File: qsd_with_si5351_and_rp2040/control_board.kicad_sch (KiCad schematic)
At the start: 33 parts, among them U101 RP2040, U102 W25Q128JVS, U103 MS5351M, Y101 403C35D12M00000, Y102 MCSJK-7U-27.00-10-10-60-B-10

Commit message: schematic ~ done - try some layout
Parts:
- added D101: LED_RED, Diode_SMD:D_0805_2012Metric, symbol Device:LED_Small
- added J104: Conn_01x04, Connector_PinHeader_2.54mm:PinHeader_1x04_P2.54mm_Vertical, symbol Connector_Generic:Conn_01x04
- added J105: Conn_02x14_Odd_Even, Connector_PinSocket_2.54mm:PinSocket_2x14_P2.54mm_Vertical, symbol Connector_Generic:Conn_02x14_Odd_Even
- added J106: Conn_01x03, Connector_PinHeader_2.54mm:PinHeader_1x03_P2.54mm_Vertical, symbol Connector_Generic:Conn_01x03
- added R106, R107: 2.2k, Resistor_SMD:R_0805_2012Metric_Pad1.20x1.40mm_HandSolder, symbol Device:R_Small
- added R109: 1K, Resistor_SMD:R_0805_2012Metric_Pad1.20x1.40mm_HandSolder, symbol Device:R_Small
- FB101: footprint Resistor_SMD:R_0805_2012Metric_Pad1.20x1.40mm_HandSolder -> Inductor_SMD:L_0805_2012Metric_Pad1.05x1.20mm_HandSolder
- FB102: value 1000ohms -> 1000; footprint Resistor_SMD:R_0805_2012Metric_Pad1.20x1.40mm_HandSolder -> Inductor_SMD:L_0805_2012Metric_Pad1.05x1.20mm_HandSolder
- J101, J102: renamed from J?; footprint (none) -> Connector_PinHeader_2.54mm:PinHeader_1x02_P2.54mm_Vertical
- J103: renamed from J?; footprint (none) -> Connector_PinHeader_2.54mm:PinHeader_1x04_P2.54mm_Vertical
- R103, R104, R105, R108: renamed from R?; footprint (none) -> Resistor_SMD:R_0805_2012Metric_Pad1.20x1.40mm_HandSolder
- gave numbers to parts that had none: 17
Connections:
- net GND: now also J105.27 (Pin_27), J105.28 (Pin_28), J106.3 (Pin_3), R109.1
- net VCC_3V3: now also J105.1 (Pin_1)
- net at C103.1, C104.1, FB102.2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: now also R106.1, R107.1
- net GPIO8: now reaches U101.11 (GPIO8)
- net GPIO8: now also J105.8 (Pin_8)
- net GPIO9: now reaches U101.12 (GPIO9)
- net GPIO9: now also J105.9 (Pin_9)
- net GPIO10: now reaches U101.13 (GPIO10)
- net GPIO10: now also J105.10 (Pin_10)
- net GPIO11: now reaches U101.14 (GPIO11)
- net GPIO11: now also J105.11 (Pin_11)
- net GPIO12: now reaches U101.15 (GPIO12)
- net GPIO12: now also J105.12 (Pin_12)
- net GPIO13: now reaches U101.16 (GPIO13)
- net GPIO13: now also J105.13 (Pin_13)
- net GPIO14: now reaches U101.17 (GPIO14)
- net GPIO14: now also J105.14 (Pin_14)
- net GPIO15: now reaches U101.18 (GPIO15)
- net GPIO15: now also J105.15 (Pin_15)
- net UART0_TX: now reaches U101.2 (GPIO0)
- net UART0_TX: now also J106.1 (Pin_1)
- net GPIO16: now reaches U101.27 (GPIO16)
- net GPIO16: now also J105.16 (Pin_16)
- net GPIO17: now reaches U101.28 (GPIO17)
- net GPIO17: now also J105.17 (Pin_17)
- net GPIO18: now reaches U101.29 (GPIO18)
- net GPIO18: now also J105.18 (Pin_18)
- net UART0_RX: now reaches U101.3 (GPIO1)
- net UART0_RX: now also J106.2 (Pin_2)
- net GPIO19: now reaches U101.30 (GPIO19)
- net GPIO19: now also J105.19 (Pin_19)
- net GPIO20: now reaches U101.31 (GPIO20)
- net GPIO20: now also J105.20 (Pin_20)
- net GPIO21: now reaches U101.32 (GPIO21)
- net GPIO21: now also J105.21 (Pin_21)
- net GPIO22: now reaches U101.34 (GPIO22)
- net GPIO22: now also J105.22 (Pin_22)
- net GPIO23: now reaches U101.35 (GPIO23)
- net GPIO23: now also J105.23 (Pin_23)
- net GPIO24: now reaches U101.36 (GPIO24)
- net GPIO24: now also J105.24 (Pin_24)
- net at U101.37 (GPIO25): now also D101.2 (A)
- net ADC_0: now reaches U101.38 (GPIO26_ADC0)
- net ADC_0: now also J104.1 (Pin_1)
- net ADC_1: now reaches U101.39 (GPIO27_ADC1)
- net ADC_1: now also J104.2 (Pin_2)
- net GPIO2: now reaches U101.4 (GPIO2)
- net GPIO2: now also J105.2 (Pin_2)
- net ADC_2: now reaches U101.40 (GPIO28_ADC2)
- net ADC_2: now also J104.3 (Pin_3)
- net ADC_3: now reaches U101.41 (GPIO29_ADC3)
- net ADC_3: now also J104.4 (Pin_4)
- net GPIO3: now reaches U101.5 (GPIO3)
- net GPIO3: now also J105.3 (Pin_3)
- net GPIO4: now reaches U101.6 (GPIO4)
- net GPIO4: now also U103.5 (SDA), J105.4 (Pin_4), R106.2
- net GPIO5: now reaches U101.7 (GPIO5)
- net GPIO5: now also U103.4 (SCL), J105.5 (Pin_5), R107.2
- net GPIO6: now reaches U101.8 (GPIO6)
- net GPIO6: now also J105.6 (Pin_6)
- net GPIO7: now reaches U101.9 (GPIO7)
- net GPIO7: now also J105.7 (Pin_7)
- new net: D101.1 (K), R109.2
- new net ANALOG_VCC: J105.26 (Pin_26)
- new net USB_5V: J105.25 (Pin_25)
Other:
- moved on the sheet: C102, C103, C104, FB101, FB102, J102, J103, R104, U103, Y102

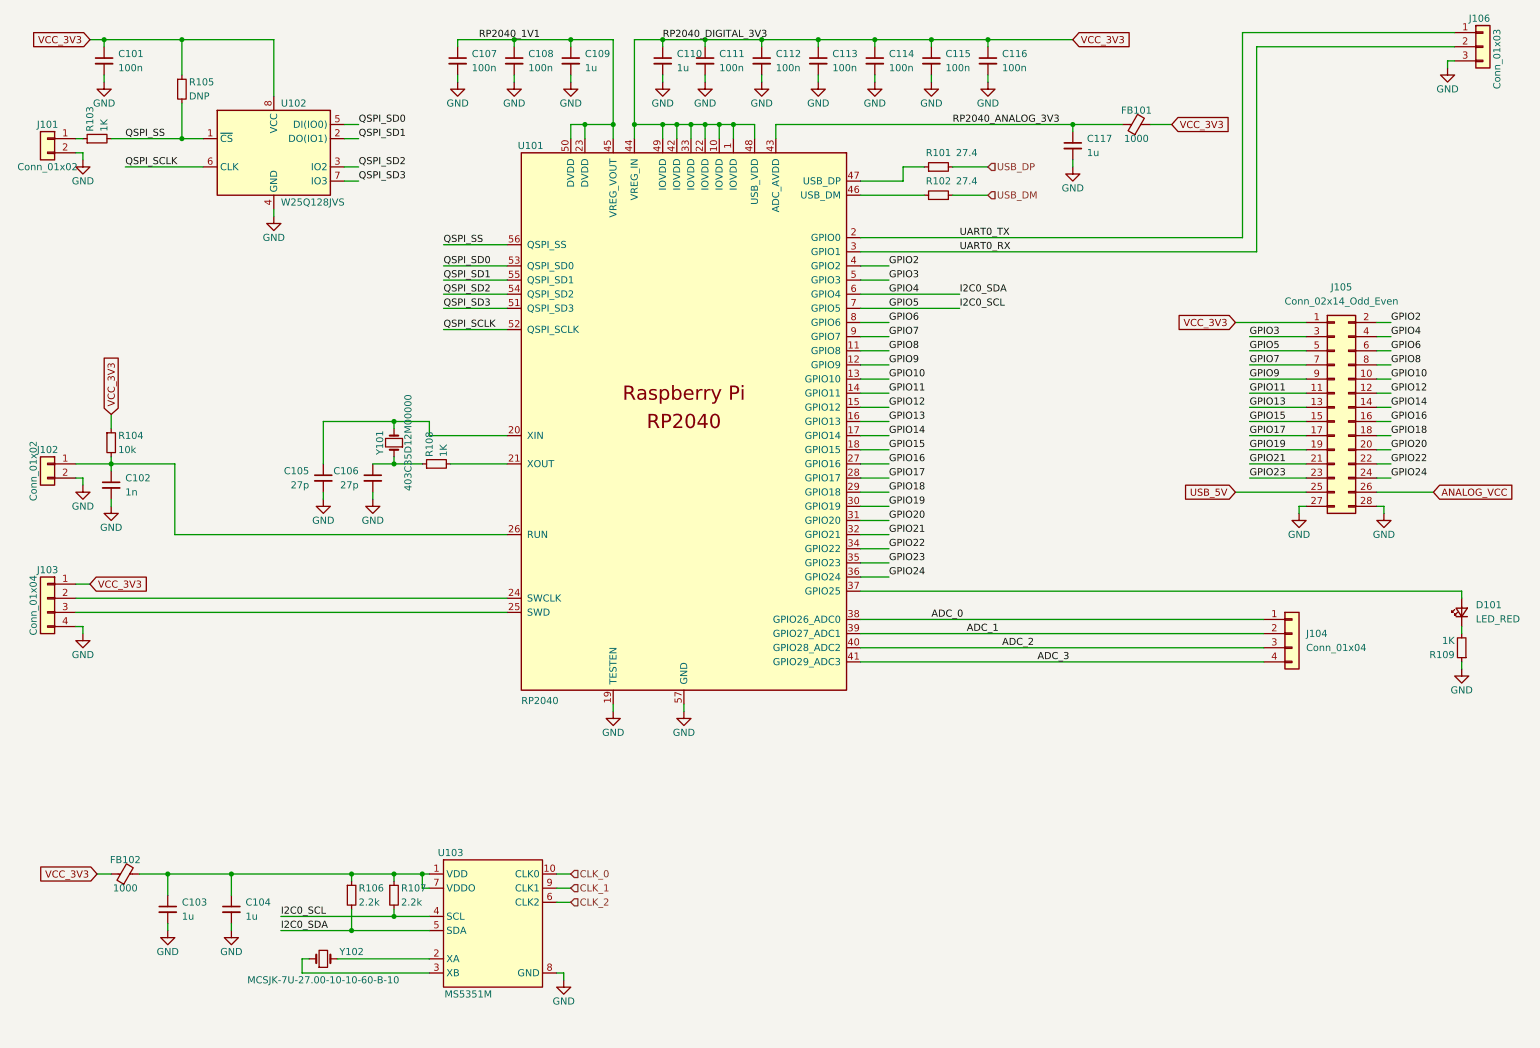
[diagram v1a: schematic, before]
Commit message: version with stackable connector
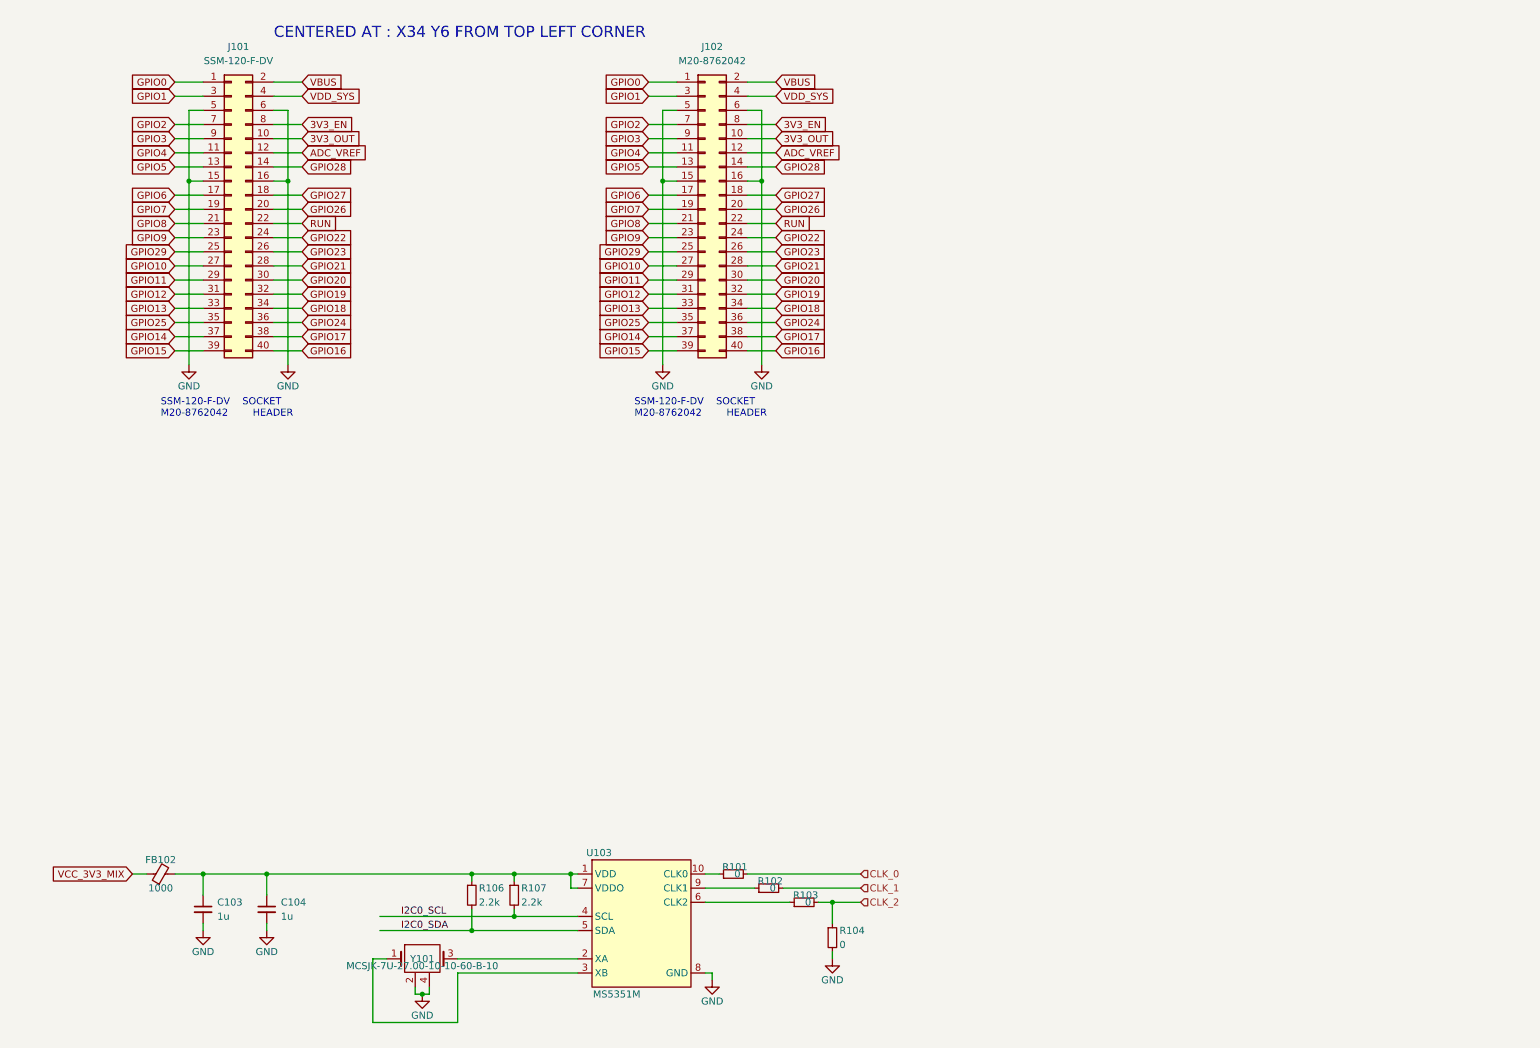
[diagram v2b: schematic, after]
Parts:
- removed C101, C107, C108, C111, C112, C113, C114, C115, C116: 100n, Capacitor_SMD:C_0805_2012Metric, symbol Device:C_Small
- removed C102: 1n, Capacitor_SMD:C_0805_2012Metric, symbol Device:C_Small
- removed C105, C106: 27p, Capacitor_SMD:C_0805_2012Metric, symbol Device:C_Small
- removed C109, C110, C117: 1u, Capacitor_SMD:C_0805_2012Metric, symbol Device:C_Small
- removed D101: LED_RED, Diode_SMD:D_0805_2012Metric, symbol Device:LED_Small
- removed FB101: 1000, Inductor_SMD:L_0805_2012Metric_Pad1.05x1.20mm_HandSolder, symbol Device:FerriteBead_Small
- removed J101, J102: Conn_01x02, Connector_PinHeader_2.54mm:PinHeader_1x02_P2.54mm_Vertical, symbol Connector_Generic:Conn_01x02
- removed J103, J104: Conn_01x04, Connector_PinHeader_2.54mm:PinHeader_1x04_P2.54mm_Vertical, symbol Connector_Generic:Conn_01x04
- removed J105: Conn_02x14_Odd_Even, Connector_PinSocket_2.54mm:PinSocket_2x14_P2.54mm_Vertical, symbol Connector_Generic:Conn_02x14_Odd_Even
- removed J106: Conn_01x03, Connector_PinHeader_2.54mm:PinHeader_1x03_P2.54mm_Vertical, symbol Connector_Generic:Conn_01x03
- removed R105: DNP, Resistor_SMD:R_0805_2012Metric_Pad1.20x1.40mm_HandSolder, symbol Device:R_Small
- removed R108, R109: 1K, Resistor_SMD:R_0805_2012Metric_Pad1.20x1.40mm_HandSolder, symbol Device:R_Small
- removed U101: RP2040, MCU_RaspberryPi_and_Boards:RP2040-QFN-56, symbol MCU_RaspberryPi_and_Boards:RP2040
- removed U102: W25Q128JVS, Package_SO:SOIC-8_5.23x5.23mm_P1.27mm, symbol Memory_Flash:W25Q128JVS
- removed Y101: 403C35D12M00000, Crystal:Crystal_SMD_3225-4Pin_3.2x2.5mm, symbol Device:Crystal_Small
- removed Y102: MCSJK-7U-27.00-10-10-60-B-10, Crystal:Crystal_SMD_3225-4Pin_3.2x2.5mm, symbol Device:Crystal_Small
- added J101: SSM-120-F-DV, Connector_PinSocket_2.54mm:PinSocket_2x20_P2.54mm_Vertical_SMD, symbol Connector_Generic:Conn_02x20_Odd_Even
- added J102: M20-8762042, Connector_PinHeader_2.54mm:PinHeader_2x20_P2.54mm_Vertical_SMD, symbol Connector_Generic:Conn_02x20_Odd_Even
- added Y101: MCSJK-7U-27.00-10-10-60-B-10, Crystal:Crystal_SMD_3225-4Pin_3.2x2.5mm, symbol parts:MCSJK-7U-27.00-10-10-60-B-10
- R101, R102: value 27.4 -> 0
- R103: value 1K -> 0
- R104: value 10k -> 0
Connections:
- net QSPI_SS is gone; now on net CLK_2: R103.2
- net USB_DM is gone; now on net CLK_1: R102.2
- net USB_DP is gone; now on net CLK_0: R101.2
- net CLK_0: no longer U103.10 (CLK0)
- net CLK_1: no longer U103.9 (CLK1)
- net CLK_2: now also R104.1; no longer U103.6 (CLK2)
- net GND: now also R104.2, J101.15 (Pin_15), J101.16 (Pin_16), J101.5 (Pin_5), J101.6 (Pin_6), J102.15 (Pin_15), J102.16 (Pin_16), J102.5 (Pin_5), J102.6 (Pin_6), Y101.2, Y101.4
- net GPIO10: now also J101.27 (Pin_27), J102.27 (Pin_27)
- net GPIO11: now also J101.29 (Pin_29), J102.29 (Pin_29)
- net GPIO12: now also J101.31 (Pin_31), J102.31 (Pin_31)
- net GPIO13: now also J101.33 (Pin_33), J102.33 (Pin_33)
- net GPIO14: now also J101.37 (Pin_37), J102.37 (Pin_37)
- net GPIO15: now also J101.39 (Pin_39), J102.39 (Pin_39)
- net GPIO16: now also J101.40 (Pin_40), J102.40 (Pin_40)
- net GPIO17: now also J101.38 (Pin_38), J102.38 (Pin_38)
- net GPIO18: now also J101.34 (Pin_34), J102.34 (Pin_34)
- net GPIO19: now also J101.32 (Pin_32), J102.32 (Pin_32)
- net GPIO2: now also J101.7 (Pin_7), J102.7 (Pin_7)
- net GPIO20: now also J101.30 (Pin_30), J102.30 (Pin_30)
- net GPIO21: now also J101.28 (Pin_28), J102.28 (Pin_28)
- net GPIO22: now also J101.24 (Pin_24), J102.24 (Pin_24)
- net GPIO23: now also J101.26 (Pin_26), J102.26 (Pin_26)
- net GPIO24: now also J101.36 (Pin_36), J102.36 (Pin_36)
- net GPIO3: now also J101.9 (Pin_9), J102.9 (Pin_9)
- net GPIO4: now also J101.11 (Pin_11), J102.11 (Pin_11); no longer R106.2, U103.5 (SDA)
- net GPIO5: now also J101.13 (Pin_13), J102.13 (Pin_13); no longer R107.2, U103.4 (SCL)
- net GPIO6: now also J101.17 (Pin_17), J102.17 (Pin_17)
- net GPIO7: now also J101.19 (Pin_19), J102.19 (Pin_19)
- net GPIO8: now also J101.21 (Pin_21), J102.21 (Pin_21)
- net GPIO9: now also J101.23 (Pin_23), J102.23 (Pin_23)
- net at R102.1: now also U103.9 (CLK1)
- net at R103.1: now also U103.6 (CLK2)
- net at R101.1: now also U103.10 (CLK0)
- net at U103.3 (XB): now also Y101.1
- net at U103.2 (XA): now also Y101.3
- net VCC_3V3 renamed VCC_3V3_MIX
- net VCC_3V3_MIX: no longer R104.1
- new net 3V3_EN: J101.8 (Pin_8), J102.8 (Pin_8)
- new net 3V3_OUT: J101.10 (Pin_10), J102.10 (Pin_10)
- new net ADC_VREF: J101.12 (Pin_12), J102.12 (Pin_12)
- new net GPIO0: J101.1 (Pin_1), J102.1 (Pin_1)
- new net GPIO1: J101.3 (Pin_3), J102.3 (Pin_3)
- new net GPIO25: J101.35 (Pin_35), J102.35 (Pin_35)
- new net GPIO26: J101.20 (Pin_20), J102.20 (Pin_20)
- new net GPIO27: J101.18 (Pin_18), J102.18 (Pin_18)
- new net GPIO28: J101.14 (Pin_14), J102.14 (Pin_14)
- new net GPIO29: J101.25 (Pin_25), J102.25 (Pin_25)
- new net I2C0_SCL: R107.2, U103.4 (SCL)
- new net I2C0_SDA: R106.2, U103.5 (SDA)
- new net RUN: J101.22 (Pin_22), J102.22 (Pin_22)
- new net VBUS: J101.2 (Pin_2), J102.2 (Pin_2)
- new net VDD_SYS: J101.4 (Pin_4), J102.4 (Pin_4)
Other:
- note added: "CENTERED AT : X34 Y6 FROM TOP LEFT CORNER"
- note added: "SSM-120-F-DV SOCKET M20-8762042 HEADER"
- moved on the sheet: C103, C104, FB102, R106, R107, U103
